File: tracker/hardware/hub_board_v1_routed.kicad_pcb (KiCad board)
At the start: 2 copper layers, 50 x 40 mm, 30 parts, among them U1 RP2040-Zero, U2 LoRa2021, U3 MAX-M10S, U4 MS5611, U5 TPS7A02

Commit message: feat(hardware): 4-layer board with In1.Cu GND plane, In2.Cu 3V3 plane, signals on F.Cu/B.Cu
- Fixed route_4layer.py: pcbnew.PCB_ZONE(b) → pcbnew.ZONE(b) (2 occurrences)
- Fixed net code lookup: use pad.GetNetCode() for signal nets where FindNet returns SwigPyObject
- Generated hub_board_v1_4layer.kicad_pcb: 4 copper layers, 30 footprints, 87 tracks, 2 zones
- GND zone on In1.Cu (layer 4), 3V3 zone on In2.Cu (layer 6)
- 39 thermal vias for power nets (23 GND + 16 3V3)
- 48 signal tracks on F.Cu/B.Cu (alternating layers)
- DRC: 450 violations (solder_mask_bridge warnings), 29 unconnected items
- Verified: 4 copper layers confirmed via pcbnew.LoadBoard
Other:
- copper layers 2 -> 4

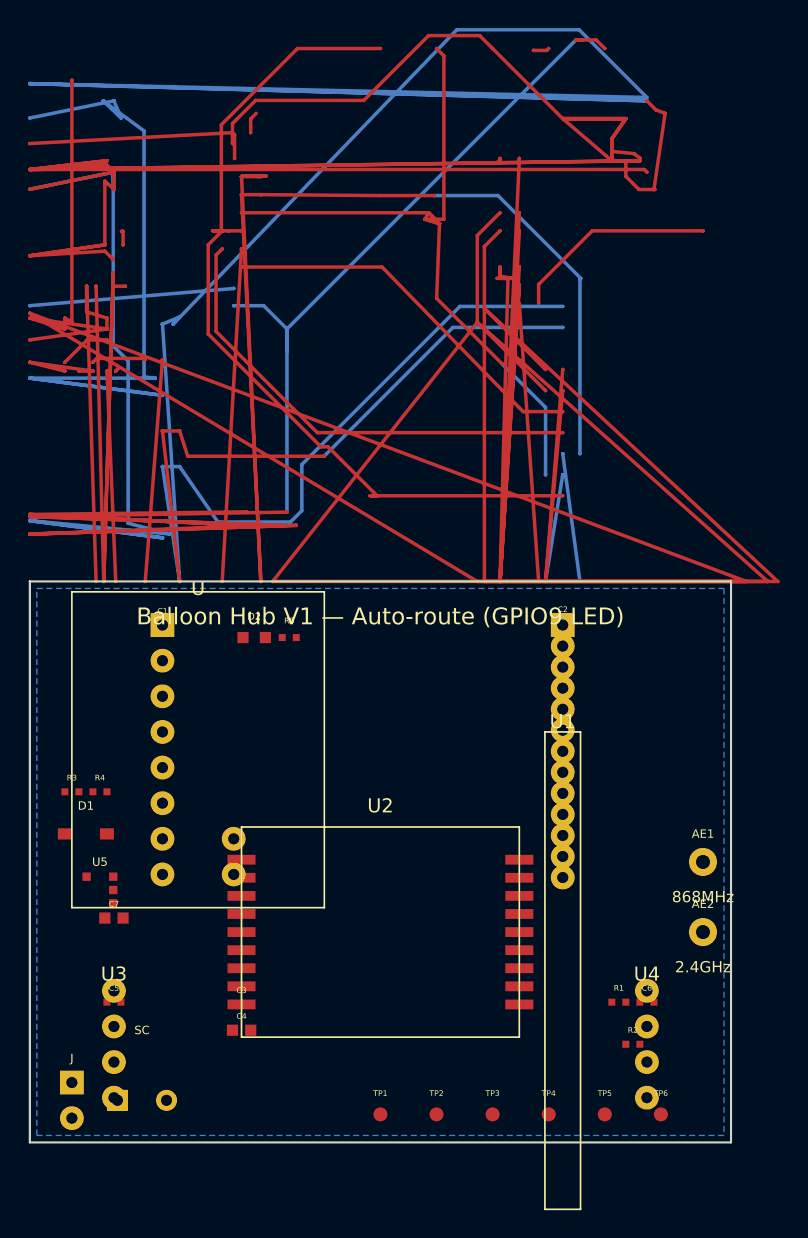
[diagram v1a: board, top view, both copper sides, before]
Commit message: fix(pcb): correct DSN track import — Y inversion + degenerate-segment collapse
Phase 1 of PCB-AUTOROUTE-EXECUTION-PLAN. The stale hub_board_v1_routed.kicad_pcb
was built by a hand-rolled DSN parser with two defects: Y was never negated
relative to KiCad coordinates (1221/1302 endpoints off-board, 58
copper_edge_clearance), and the Freerouting exporter's jittered ~0.1um duplicate
vertices were imported verbatim (181 track_dangling).

import_tracks_fixed.py makes KiCad's own ImportSpecctraSES the primary path
(route of record, coordinate-correct by construction) and keeps the DSN parser as
an explicit, source-reporting fallback; it re-measures the written file rather
than trusting its own conversion.

DRC 405 -> 175, track_dangling 181 -> 0, tracks_crossing 0, copper_edge_clearance
0. Gate: DRC < 230 PASS. 22 new tests in tests/test_pcb_track_import.py, wired
into make test-unit.
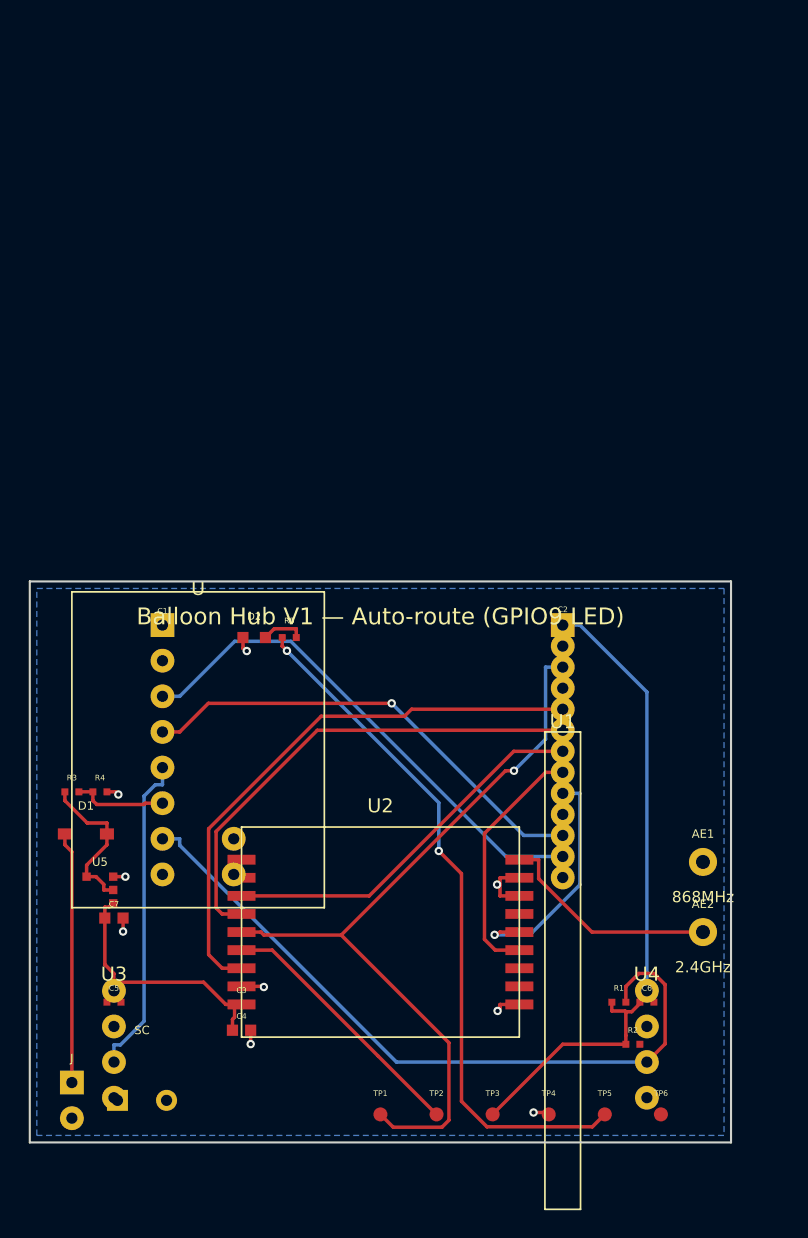
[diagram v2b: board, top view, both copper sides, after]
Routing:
- net GND: track 1405.9 -> 13.7 mm, vias 0 -> 9
- net I2C_SDA: track 433.4 -> 52.1 mm
- net 3V3: track 0.00 -> 66.7 mm
- net SPI0_SCK: track 0.00 -> 55.8 mm, vias 0 -> 1
- net STATUS_LED: track 2.31 -> 49.7 mm, vias 0 -> 2
- net ESP_TX_RP2040_RX: track 0.00 -> 36.5 mm
- net SPI0_NSS: track 0.00 -> 35.1 mm
- net LR2021_BUSY: track 0.00 -> 27.2 mm
- net GPS_TX_ESP_RX: track 0.00 -> 23.0 mm
- net SOLAR_IN: track 0.00 -> 17.9 mm
- net LR2021_DIO9: track 0.00 -> 17.7 mm
- net LR2021_RST: track 0.00 -> 17.1 mm, vias 0 -> 1
- net RP2040_TX_ESP_RX: track 20.8 -> 33.3 mm, vias 0 -> 1
- net VCAP: track 0.00 -> 11.2 mm
- net SPI0_MOSI: track 9.18 -> 18.8 mm
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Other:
- copper layers 4 -> 2
